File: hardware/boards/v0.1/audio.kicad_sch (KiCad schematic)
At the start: 45 parts, among them J4 SPKR_L, J5 SPKR_R, J8 LINE_OUT, J9 LINE_IN, U24 MIC, U28 TS5A23159RSE, U29 NAU88C22YG, U30 SI4704-D60-GM, U34 SI4710-B30-GMR, Y3 ASVK-32.768KHZ-LJ-T

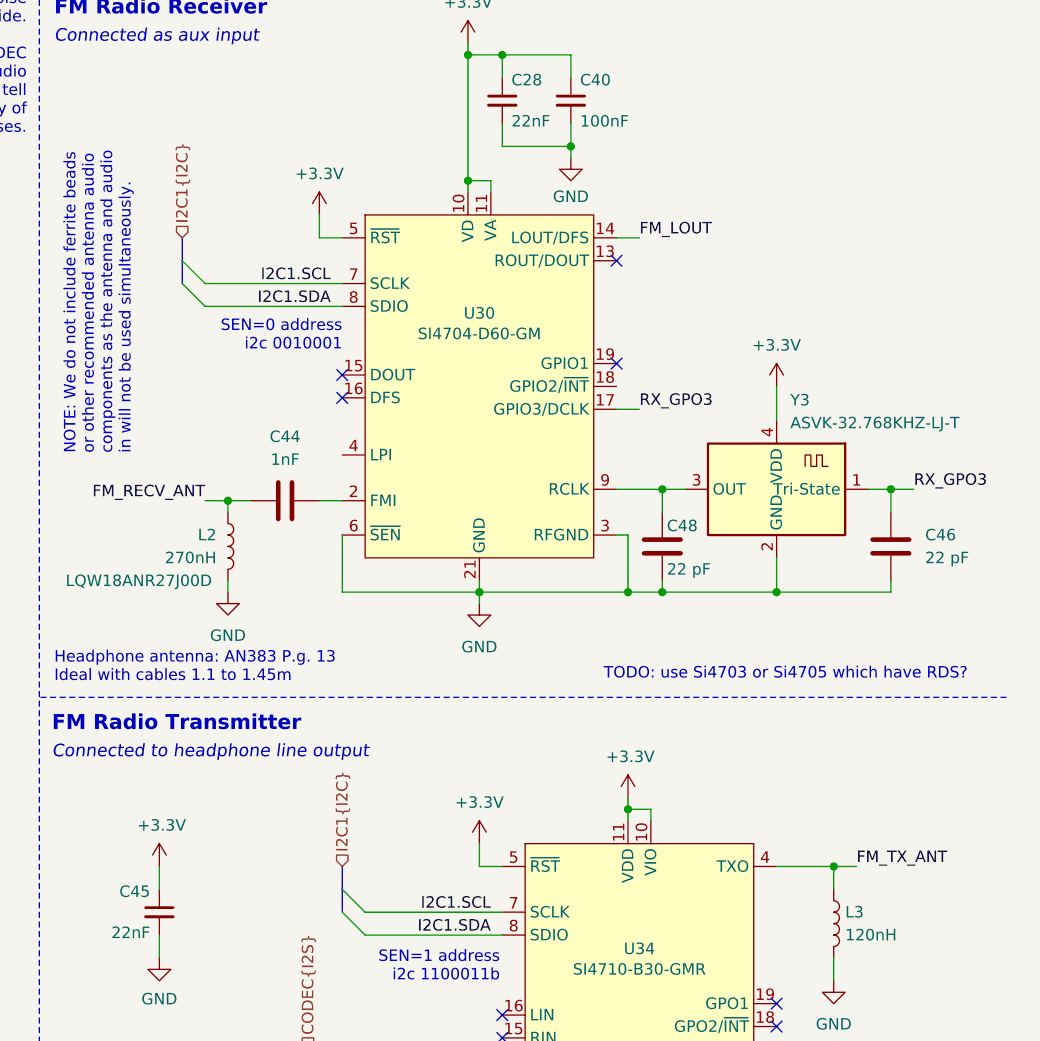
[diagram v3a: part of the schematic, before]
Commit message: feat: add FM reset pins, add fiducials
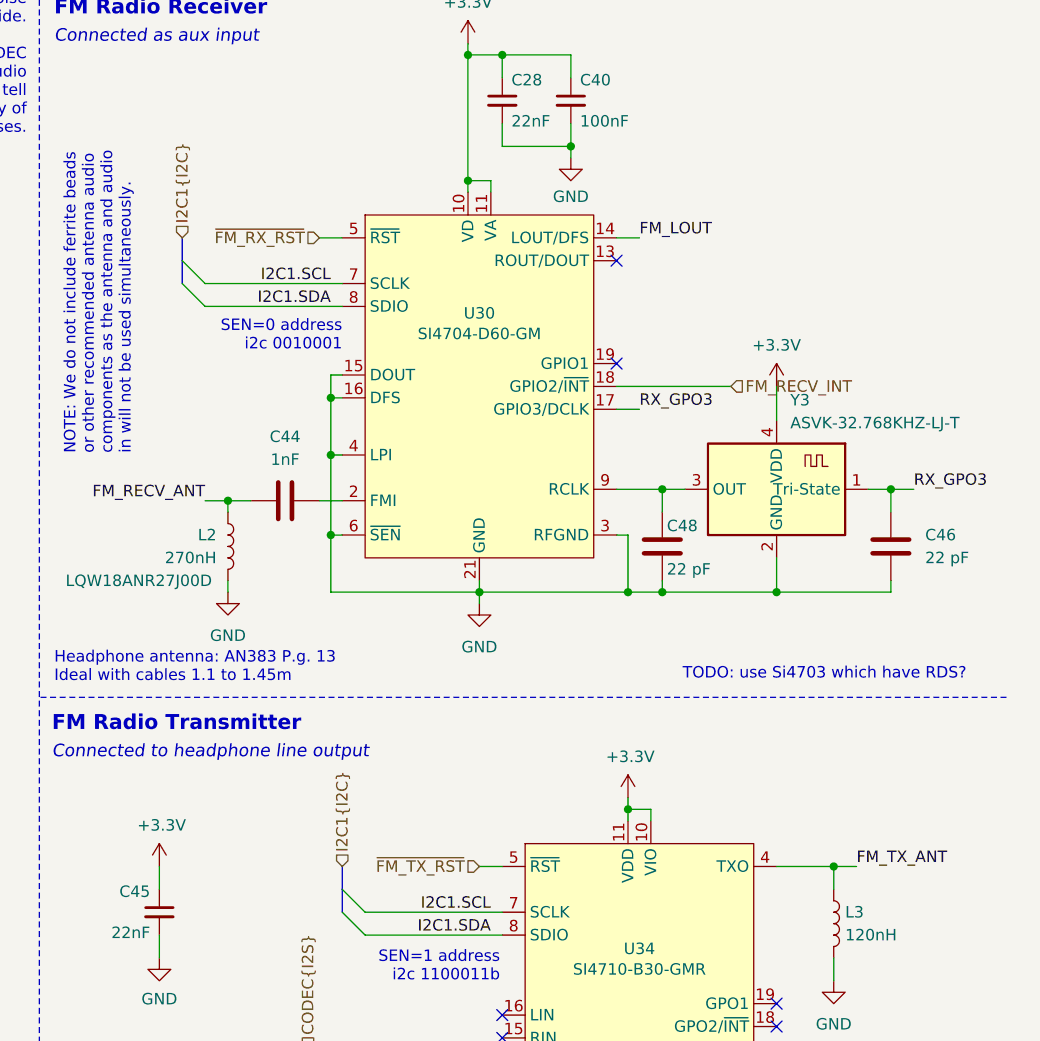
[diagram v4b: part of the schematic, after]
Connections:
- net +3.3V: no longer U30.5 (~{RST}), U34.5 (~{RST})
- net GND: now also U30.15 (DOUT), U30.16 (DFS), U30.4 (LPI)
- net FM_RECV_INT: now reaches U30.18 (GPIO2/~{INT})
- new net ~{FM_RX_RST}: U30.5 (~{RST})
- new net ~{FM_TX_RST}: U34.5 (~{RST})
- no-connect marks 11 -> 9
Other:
- note added: "TODO: use Si4703 which have RDS?"
- note removed: "TODO: use Si4703 or Si4705 which have RDS?"
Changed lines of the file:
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@@
 		)
 	)
-	(text "TODO: use Si4703 or Si4705 which have RDS?"
+	(text "TODO: use Si4703 which have RDS?"
 		(exclude_from_sim no)
-		(at 260.096 89.154 0)
+		(at 264.414 89.154 0)
 		(effects
 			(font
@@
 	)
 	(junction
+		(at 209.55 64.77)
+		(diameter 0)
+		(color 0 0 0 0)
+	)
+	(junction
 		(at 129.54 170.18)
 		(diameter 0)
@@
 	)
 	(junction
+		(at 209.55 73.66)
+		(diameter 0)
+		(color 0 0 0 0)
+	)
+	(junction
 		(at 80.01 24.13)
 		(diameter 0)
@@
 	)
 	(junction
+		(at 209.55 58.42)
+		(diameter 0)
+		(color 0 0 0 0)
+	)
+	(junction
 		(at 81.28 128.27)
 		(diameter 0)
@@
 	)
 	(no_connect
-		(at 210.82 58.42)
-	)
-	(no_connect
-		(at 210.82 55.88)
-	)
-	(no_connect
 		(at 259.08 140.97)
 	)
@@
 	(wire
 		(pts
+			(xy 209.55 58.42) (xy 209.55 64.77)
+		)
+		(stroke
+			(width 0)
+			(type default)
+		)
+	)
+	(wire
+		(pts
 			(xy 161.29 125.73) (xy 165.1 125.73)
 		)
@@
 	(wire
 		(pts
+			(xy 241.3 57.15) (xy 254 57.15)
+		)
+		(stroke
+			(width 0)
+			(type default)
+		)
+	)
+	(wire
+		(pts
 			(xy 67.31 34.29) (xy 67.31 36.83)
 		)
@@
 	(wire
 		(pts
+			(xy 210.82 64.77) (xy 209.55 64.77)
+		)
+		(stroke
+			(width 0)
+			(type default)
+		)
+	)
+	(wire
+		(pts
 			(xy 99.06 34.29) (xy 99.06 36.83)
 		)
@@
 	(wire
 		(pts
+			(xy 210.82 55.88) (xy 209.55 55.88)
+		)
+		(stroke
+			(width 0)
+			(type default)
+		)
+	)
+	(wire
+		(pts
 			(xy 120.65 90.17) (xy 120.65 92.71)
 		)
@@
 	(wire
 		(pts
-			(xy 226.06 107.95) (xy 226.06 110.49)
-		)
-		(stroke
-			(width 0)
-			(type default)
-		)
-	)
-	(wire
-		(pts
 			(xy 57.15 115.57) (xy 57.15 116.84)
 		)
@@
 	(wire
 		(pts
-			(xy 210.82 80.01) (xy 226.06 80.01)
+			(xy 209.55 80.01) (xy 226.06 80.01)
 		)
 		(stroke
@@
 	(wire
 		(pts
+			(xy 209.55 64.77) (xy 209.55 73.66)
+		)
+		(stroke
+			(width 0)
+			(type default)
+		)
+	)
+	(wire
+		(pts
 			(xy 111.76 189.23) (xy 129.54 189.23)
 		)
@@
 	(wire
 		(pts
-			(xy 210.82 73.66) (xy 210.82 80.01)
+			(xy 209.55 73.66) (xy 209.55 80.01)
 		)
 		(stroke
@@
 	(wire
 		(pts
-			(xy 208.28 38.1) (xy 208.28 40.64)
+			(xy 123.19 82.55) (xy 120.65 82.55)
 		)
 		(stroke
@@
 	(wire
 		(pts
-			(xy 123.19 82.55) (xy 120.65 82.55)
+			(xy 107.95 125.73) (xy 107.95 128.27)
 		)
 		(stroke
@@
 	(wire
 		(pts
-			(xy 107.95 125.73) (xy 107.95 128.27)
+			(xy 134.62 59.69) (xy 134.62 69.85)
 		)
 		(stroke
@@
 	(wire
 		(pts
-			(xy 134.62 59.69) (xy 134.62 69.85)
+			(xy 105.41 97.79) (xy 107.95 97.79)
 		)
 		(stroke
@@
 	(wire
 		(pts
-			(xy 105.41 97.79) (xy 107.95 97.79)
+			(xy 118.11 105.41) (xy 118.11 102.87)
 		)
 		(stroke
@@
 	(wire
 		(pts
-			(xy 118.11 105.41) (xy 118.11 102.87)
+			(xy 57.15 83.82) (xy 59.69 83.82)
 		)
 		(stroke
@@
 	(wire
 		(pts
-			(xy 57.15 83.82) (xy 59.69 83.82)
+			(xy 228.6 27.94) (xy 228.6 30.48)
 		)
 		(stroke
@@
 	(wire
 		(pts
-			(xy 228.6 27.94) (xy 228.6 30.48)
+			(xy 209.55 58.42) (xy 210.82 58.42)
 		)
 		(stroke
@@
 	(wire
 		(pts
+			(xy 209.55 73.66) (xy 210.82 73.66)
+		)
+		(stroke
+			(width 0)
+			(type default)
+		)
+	)
+	(wire
+		(pts
 			(xy 87.63 182.88) (xy 91.44 182.88)
 		)
@@
 		)
 	)
+	(wire
+		(pts
+			(xy 209.55 55.88) (xy 209.55 58.42)
+		)
+		(stroke
+			(width 0)
+			(type default)
+		)
+	)
 	(bus
 		(pts
@@
 		)
 	)
+	(hierarchical_label "~{FM_TX_RST}"
+		(shape input)
+		(at 226.06 110.49 180)
+		(effects
+			(font
+				(size 1.27 1.27)
+			)
+			(justify right)
+		)
+	)
 	(hierarchical_label "I2C1{I2C}"
 		(shape input)
@@
 		)
 	)
+	(hierarchical_label "~{FM_RX_RST}"
+		(shape input)
+		(at 208.28 40.64 180)
+		(effects
+			(font
+				(size 1.27 1.27)
+			)
+			(justify right)
+		)
+	)
+	(hierarchical_label "FM_RECV_INT"
+		(shape input)
+		(at 254 57.15 0)
+		(effects
+			(font
+				(size 1.27 1.27)
+			)
+			(justify left)
+		)
+	)
 	(symbol
 		(lib_id "power:GND")
@@
 	(symbol
 		(lib_id "power:+3.3V")
-		(at 208.28 38.1 0)
-		(unit 1)
-		(exclude_from_sim no)
-		(in_bom yes)
-		(on_board yes)
-		(dnp no)
-		(property "Reference" "#PWR083"
-			(at 208.28 41.91 0)
-			(effects
-				(font
-					(size 1.27 1.27)
-				)
-				(hide yes)
-			)
-		)
-		(property "Value" "+3.3V"
-			(at 208.28 33.528 0)
-			(effects
-				(font
-					(size 1.27 1.27)
-				)
-			)
-		)
-		(property "Footprint" ""
-			(at 208.28 38.1 0)
-			(effects
-				(font
-					(size 1.27 1.27)
-				)
-				(hide yes)
-			)
-		)
-		(property "Datasheet" ""
-			(at 208.28 38.1 0)
-			(effects
-				(font
-					(size 1.27 1.27)
-				)
-				(hide yes)
-			)
-		)
-		(property "Description" "Power symbol creates a global label with name \"+3.3V\""
-			(at 208.28 38.1 0)
-			(effects
-				(font
-					(size 1.27 1.27)
-				)
-				(hide yes)
-			)
-		)
-		(pin "1"
-		)
-		(instances
-			(project "pocket_synth"
-				(path "/485383b8-00f4-4405-b270-de249939cff4/ac7a2cd5-8a17-4132-a50f-a1edfbc58e6d"
-					(reference "#PWR083")
-					(unit 1)
-				)
-			)
-		)
-	)
-	(symbol
-		(lib_id "power:+3.3V")
 		(at 259.08 57.15 0)
 		(unit 1)
@@
 					(unit 1)
 				)
-			)
-		)
-	)
-	(symbol
-		(lib_id "power:+3.3V")
-		(at 226.06 107.95 0)
-		(unit 1)
-		(exclude_from_sim no)
-		(in_bom yes)
-		(on_board yes)
-		(dnp no)
-		(property "Reference" "#PWR084"
-			(at 226.06 111.76 0)
-			(effects
-				(font
-					(size 1.27 1.27)
-				)
-				(hide yes)
-			)
-		)
-		(property "Value" "+3.3V"
-			(at 226.06 103.378 0)
-			(effects
-				(font
-					(size 1.27 1.27)
-				)
-			)
-		)
-		(property "Footprint" ""
-			(at 226.06 107.95 0)
-			(effects
-				(font
-					(size 1.27 1.27)
-				)
-				(hide yes)
-			)
-		)
-		(property "Datasheet" ""
-			(at 226.06 107.95 0)
-			(effects
-				(font
-					(size 1.27 1.27)
-				)
-				(hide yes)
-			)
-		)
-		(property "Description" "Power symbol creates a global label with name \"+3.3V\""
-			(at 226.06 107.95 0)
-			(effects
-				(font
-					(size 1.27 1.27)
-				)
-				(hide yes)
-			)
-		)
-		(pin "1"
-		)
-		(instances
-			(project "pocket_synth"
-				(path "/485383b8-00f4-4405-b270-de249939cff4/ac7a2cd5-8a17-4132-a50f-a1edfbc58e6d"
-					(reference "#PWR084")
-					(unit 1)
-				)

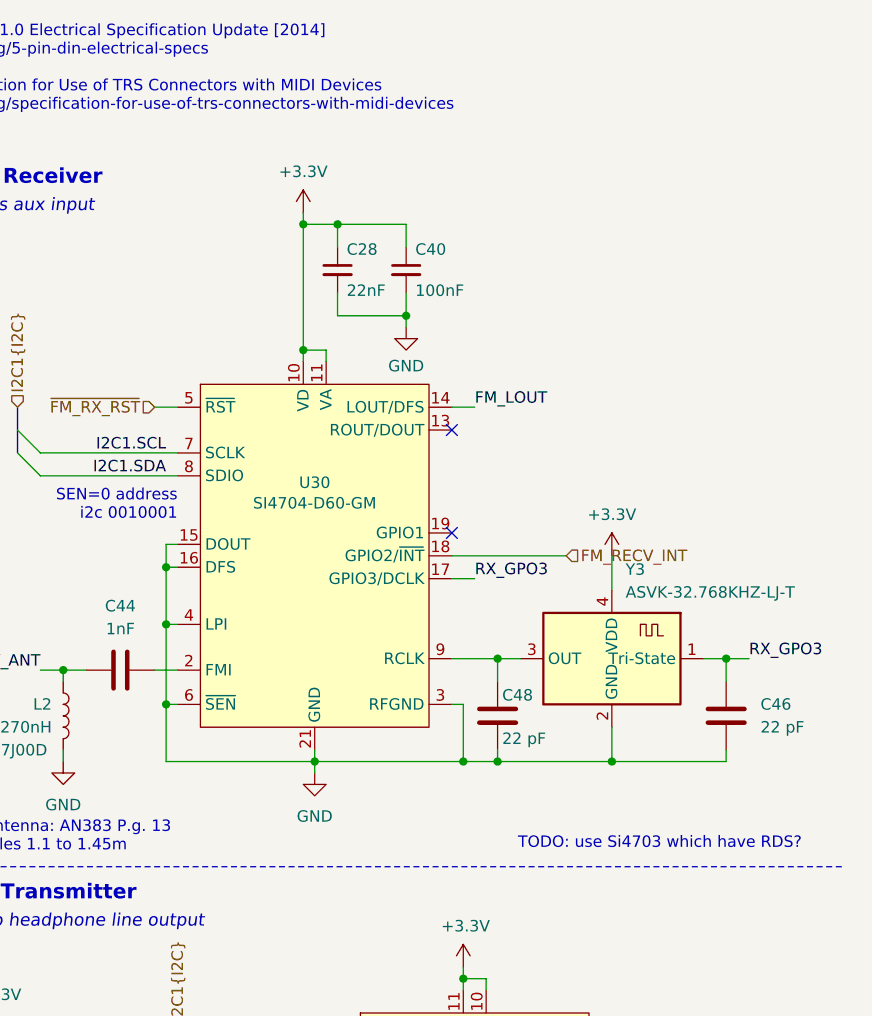
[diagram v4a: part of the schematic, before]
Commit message: feat: change FM receiver to newer model with RDS
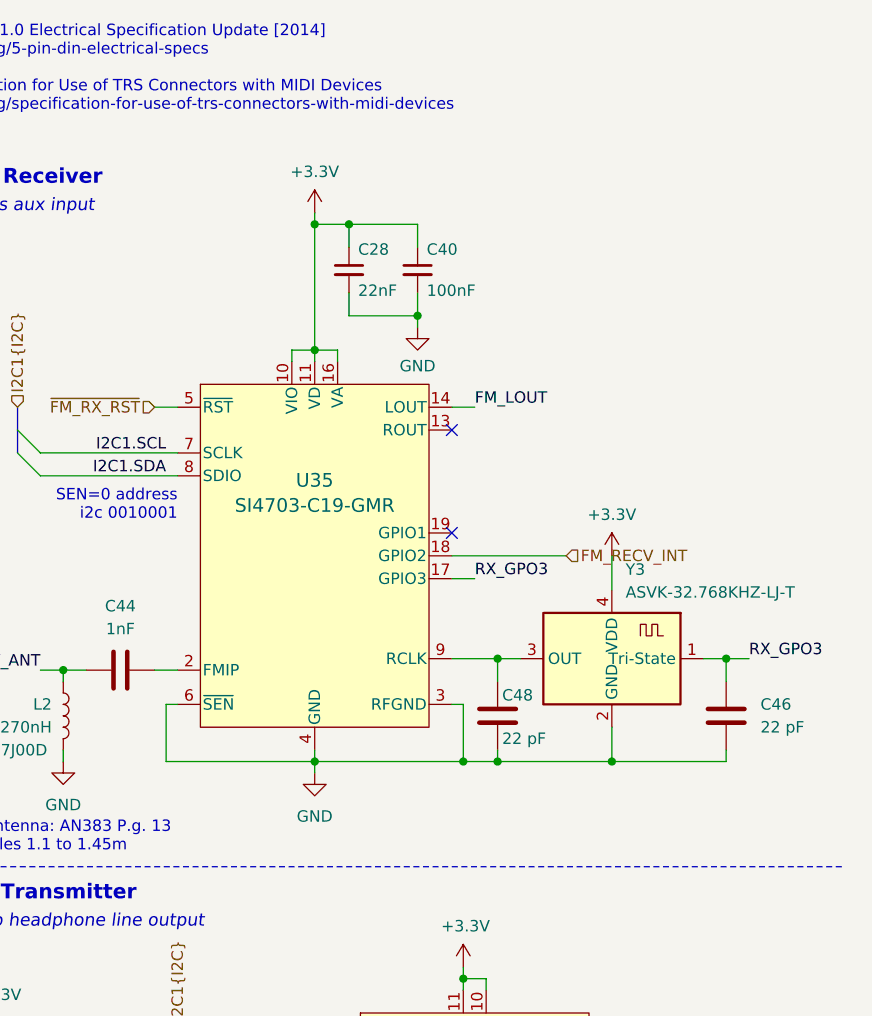
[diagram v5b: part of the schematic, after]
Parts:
- removed U30: SI4704-D60-GM, pocket_synth:SI4704-D60-GMR, symbol pocket_synth:SI4704-D60-GM
- added U35: SI4703-C19-GMR, pocket_synth:SI4703-C19-GMR, symbol pocket_synth:SI4703-C19-GMR
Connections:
- net +3.3V: now also U35.10 (VIO), U35.11 (VD), U35.16 (VA)
- net FM_LOUT: now also U35.14 (LOUT)
- net FM_RECV_INT: now also U35.18 (GPIO2)
- net I2C1.SCL: now also U35.7 (SCLK)
- net I2C1.SDA: now also U35.8 (SDIO)
- net RX_GPO3: now also U35.17 (GPIO3)
- net ~{FM_RX_RST}: now also U35.5 (~{RST})
- net at C44.2: now also U35.2 (FMIP)
- net at C48.1, Y3.3 (OUT): now also U35.9 (RCLK)
- net GND renamed EPAD
- net EPAD: now also U35.12 (GND), U35.15 (GND), U35.21 (EPAD), U35.3 (RFGND), U35.4 (GND), U35.6 (~{SEN})
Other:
- note removed: "TODO: use Si4703 which have RDS?"
- moved on the sheet: C28, C40
